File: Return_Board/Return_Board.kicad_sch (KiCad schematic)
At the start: 9 parts, among them J1 Conn_01x02_Pin, J2 Conn_01x06_Pin, U1 74HC14, U2 LM317LZ

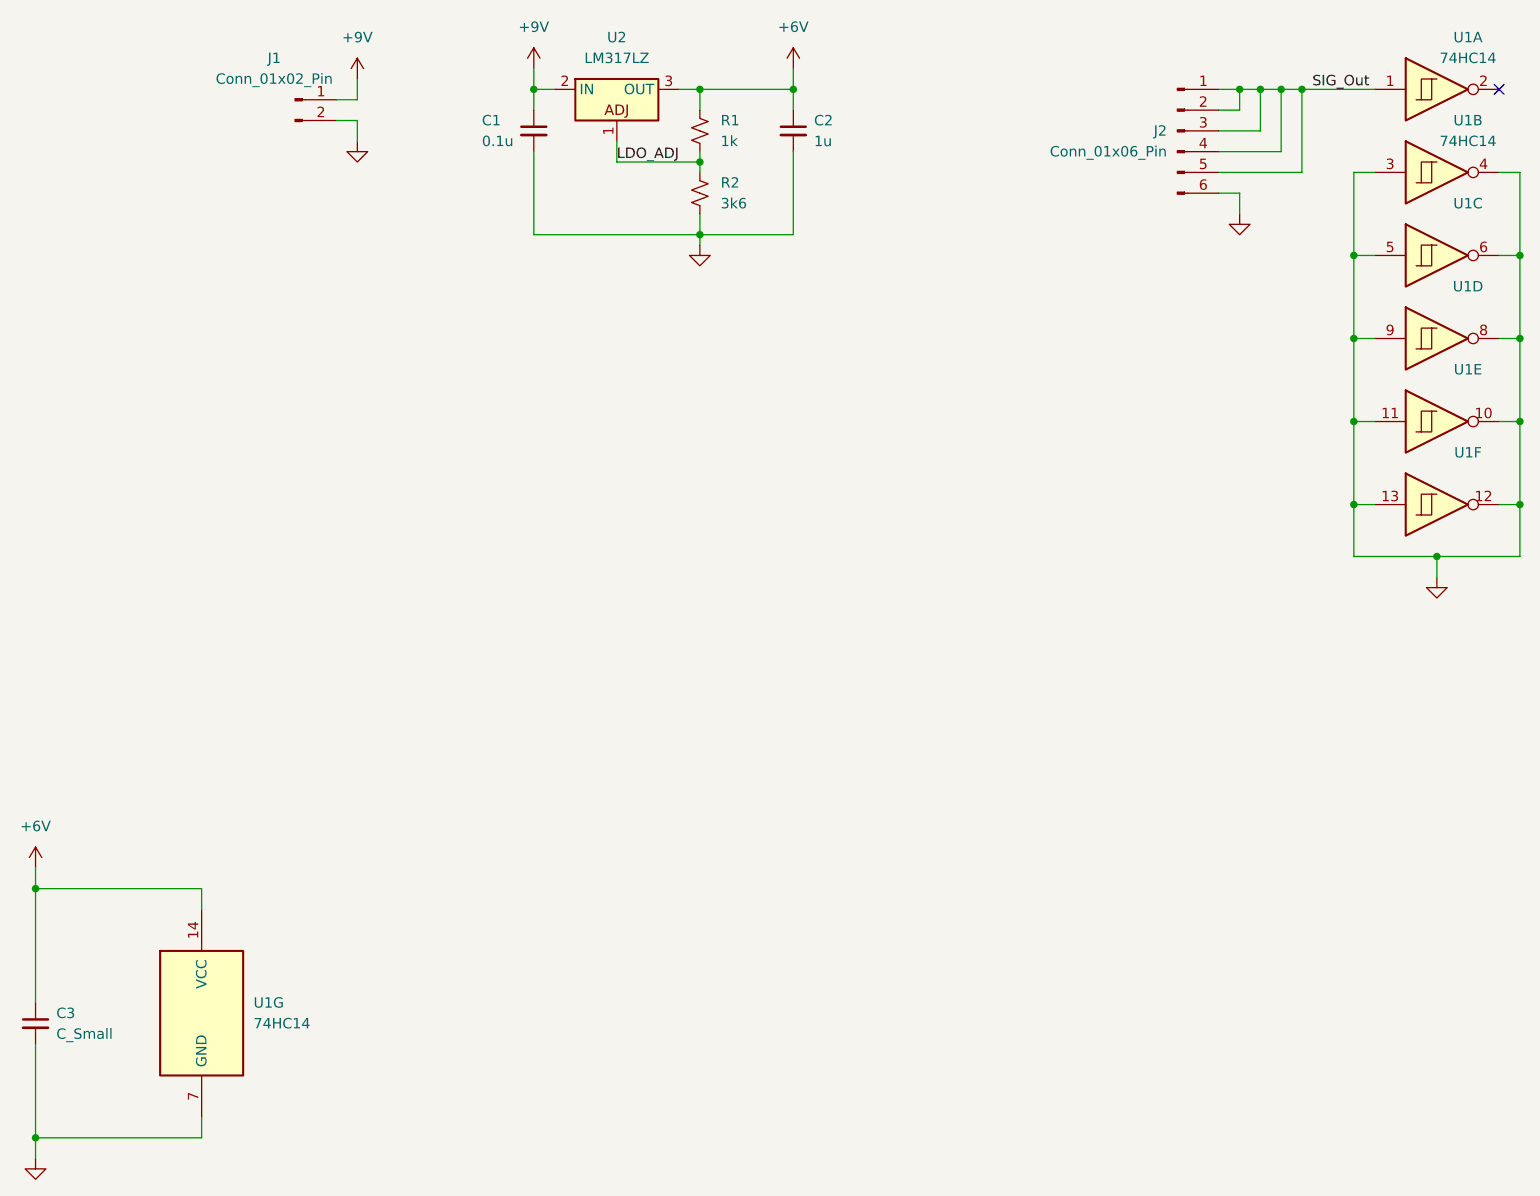
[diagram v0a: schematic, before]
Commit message: Return board version 0.0.2; updates in README
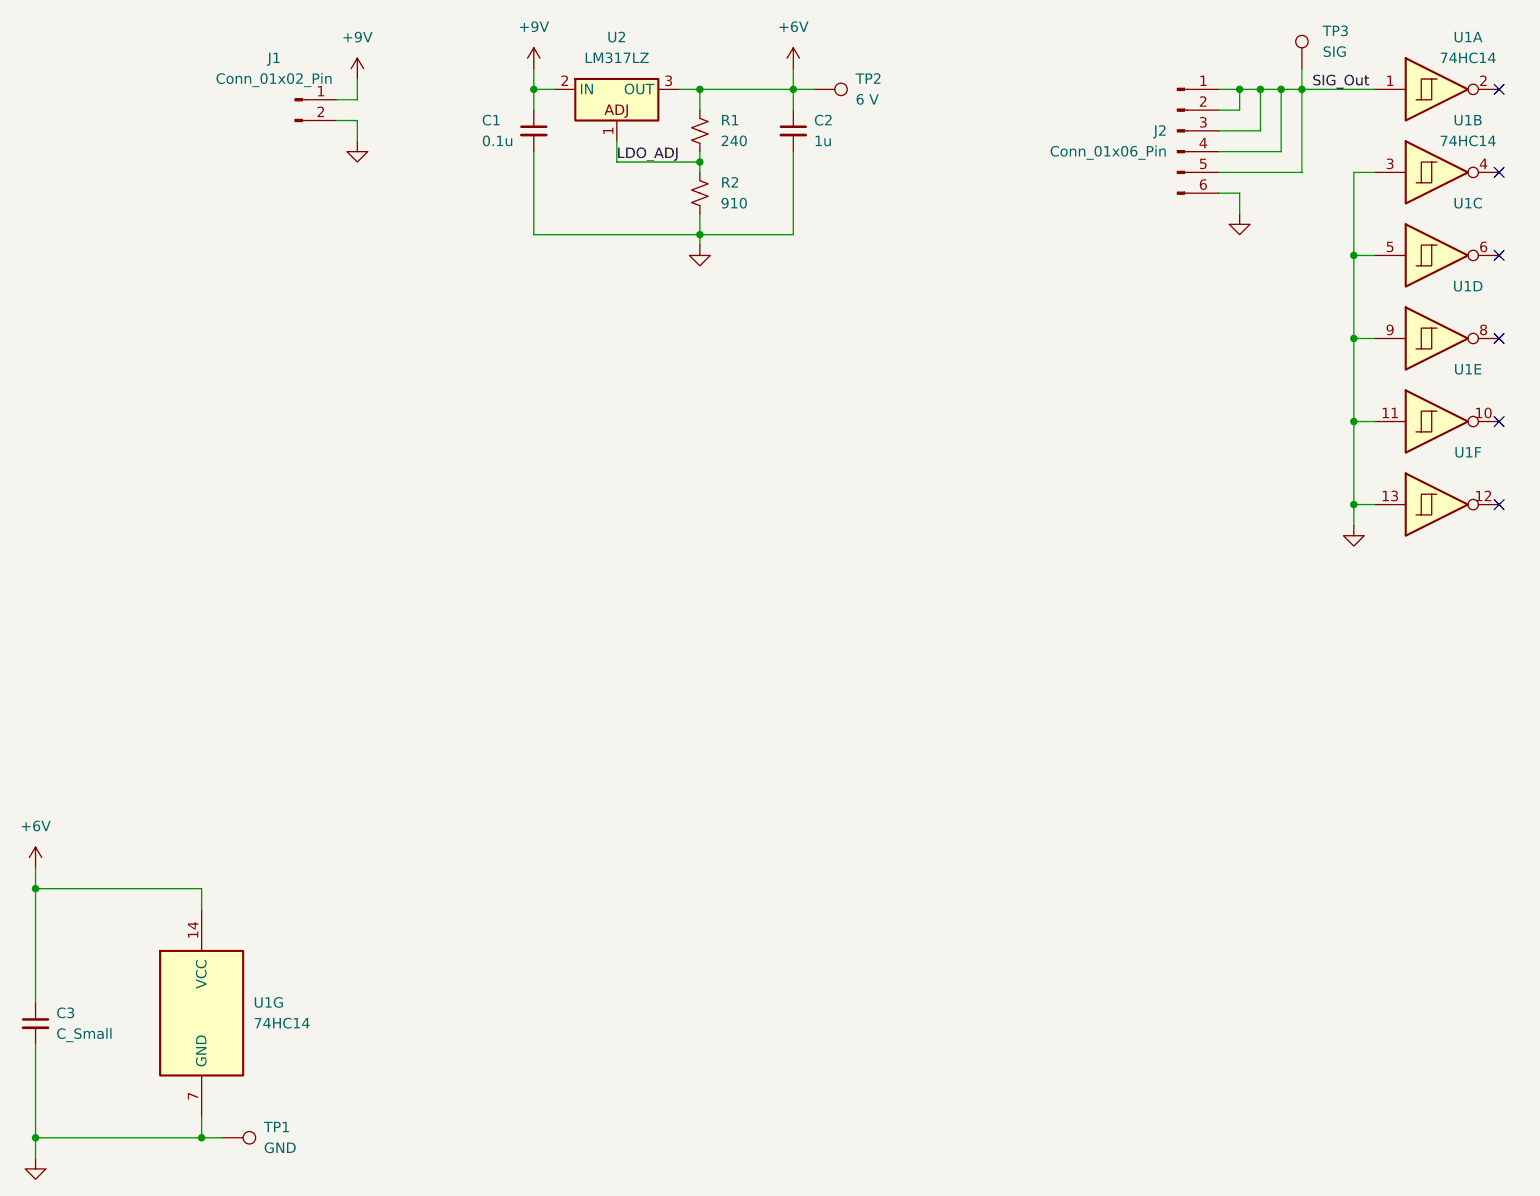
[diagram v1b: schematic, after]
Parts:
- added TP1: GND, Connector_Pin:Pin_D1.0mm_L10.0mm, symbol Connector:TestPoint
- added TP2: 6 V, Connector_Pin:Pin_D1.0mm_L10.0mm, symbol Connector:TestPoint
- added TP3: SIG, Connector_Pin:Pin_D1.0mm_L10.0mm, symbol Connector:TestPoint
- R1: value 1k -> 240; footprint PCM_Resistor_THT_AKL:R_Axial_DIN0204_L3.6mm_D1.6mm_P5.08mm_Vertical -> PCM_Resistor_THT_AKL:R_Axial_DIN0204_L3.6mm_D1.6mm_P7.62mm_Horizontal
- R2: value 3k6 -> 910; footprint PCM_Resistor_THT_AKL:R_Axial_DIN0204_L3.6mm_D1.6mm_P5.08mm_Vertical -> PCM_Resistor_THT_AKL:R_Axial_DIN0204_L3.6mm_D1.6mm_P7.62mm_Horizontal
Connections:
- net +6V: now also TP2.1
- net GND: now also TP1.1; no longer U1.10, U1.12, U1.4, U1.6, U1.8
- net SIG_Out: now also TP3.1
- no-connect marks 1 -> 6
